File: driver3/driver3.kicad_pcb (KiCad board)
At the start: 4 copper layers, 45 x 60 mm, 23 parts, among them J1 Conn_02x08_Odd_Even, J2 Conn_02x08_Counter_Clockwise, J3 Conn_01x05, J4 Conn_01x03_Pin, SW1 SW_DIP_x02, SW2 SW_DIP_x02, U1 MP6605CGR-Z

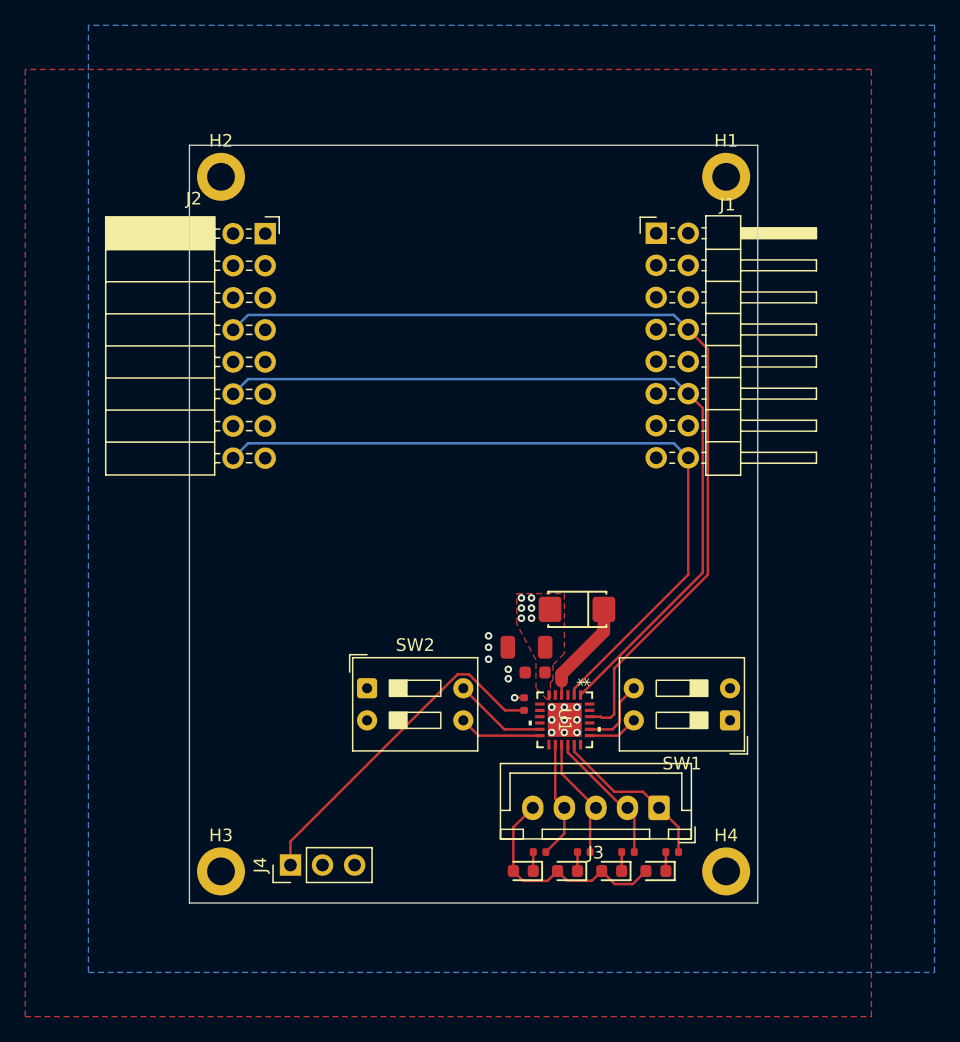
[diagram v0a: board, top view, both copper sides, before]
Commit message: Add new driver and web client
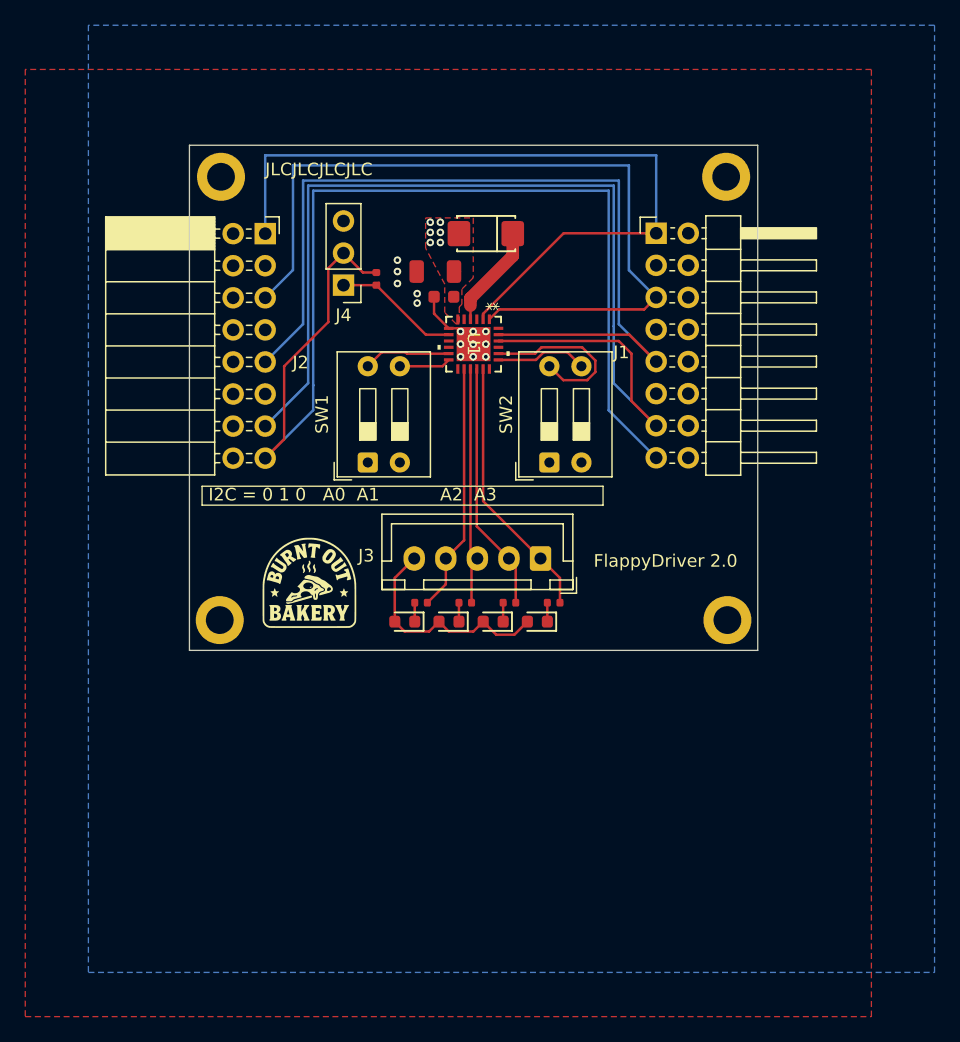
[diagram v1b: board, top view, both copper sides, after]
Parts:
- added G1: LOGO, BurntOutBakery:BurntOutBakery, F.Cu at (109.5, 85.0)
- J1: value Conn_02x08_Odd_Even -> Conn_02x08_Odd_Even_Male
- J2: value Conn_02x08_Counter_Clockwise -> Conn_02x08_Odd_Even_Female
- moved J4 46.1 mm to (112.2, 61.1), turned to 180 degrees
- moved R5 35.6 mm to (114.8, 60.6)
- moved C1 30.6 mm to (120.2, 62.0)
- moved C2 30.6 mm to (119.5, 60.0)
- moved D1 30.6 mm to (123.5, 57.0)
- moved U1 30.6 mm to (122.5, 65.8)
- moved SW2 24.9 mm to (128.5, 75.1), turned to 90 degrees
- moved D2 21.9 mm to (127.5, 87.7)
- moved D3 21.9 mm to (124.0, 87.7)
- moved D4 21.9 mm to (120.5, 87.7)
- moved J3 21.9 mm to (127.8, 82.7)
- moved D5 21.9 mm to (117.0, 87.7)
- moved R1 21.9 mm to (128.8, 86.2)
- moved R2 21.9 mm to (125.3, 86.2)
- moved R3 21.9 mm to (121.8, 86.2)
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- renumbered SW2 to SW1, SW1 to SW2
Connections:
- J1 pad 1: +12V -> SCL
- J1 pad 12: SDA -> +12V
- J1 pad 13: +12V -> NENBL
- J1 pad 15: GND -> +5V
- J1 pad 16: SCL -> +12V
- J1 pad 2: +5V -> GND
- J1 pad 4: NFAULT -> +12V
- J1 pad 5: +12V -> SDA
- J1 pad 8: NENBL -> +12V
- J1 pad 9: +12V -> NFAULT
- J2 pad 1: +12V -> SCL
- J2 pad 12: SDA -> +12V
- J2 pad 13: +12V -> NENBL
- J2 pad 15: GND -> +5V
- J2 pad 16: SCL -> +12V
- J2 pad 2: +5V -> GND
- J2 pad 4: NFAULT -> +12V
- J2 pad 5: +12V -> SDA
- J2 pad 8: NENBL -> +12V
- J2 pad 9: +12V -> NFAULT
- SW2 pad 3: A2 -> A3
- SW2 pad 4: A3 -> A2
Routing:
- net +5V: track 0.75 -> 90.9 mm, vias 1 -> 0
- net NFAULT: track 0.00 -> 69.5 mm
- net Net-(J4-Pin_1): track 27.0 -> 10.2 mm
- net Net-(J3-Pin_4): track 9.40 -> 19.7 mm
- net NENBL: track 73.3 -> 82.5 mm
- net Net-(J3-Pin_3): track 9.82 -> 18.9 mm
- net Net-(J3-Pin_2): track 10.9 -> 19.8 mm
- net A2: track 5.76 -> 13.6 mm
- net Net-(J3-Pin_1): track 13.2 -> 21.0 mm
- net GND: track 0.00 -> 5.47 mm
- net A3: track 4.00 -> 7.27 mm
- net A1: track 6.56 -> 4.08 mm
- net SDA: track 65.4 -> 63.3 mm
- net SCL: track 59.5 -> 60.1 mm
- added copper zone on B.Cu, net GND
- removed copper zone on B.Cu, net +5V
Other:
- board size 45 x 60 mm -> 45 x 40 mm
- board text added: "FlappyDriver 2.0"
- board text added: "I2C = 0 1 0 A0 A1 A2 A3"
- board text added: "JLCJLCJLCJLC"

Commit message: Go back to DRV8804 based design because the MP6605CGR seems to be out of stock.
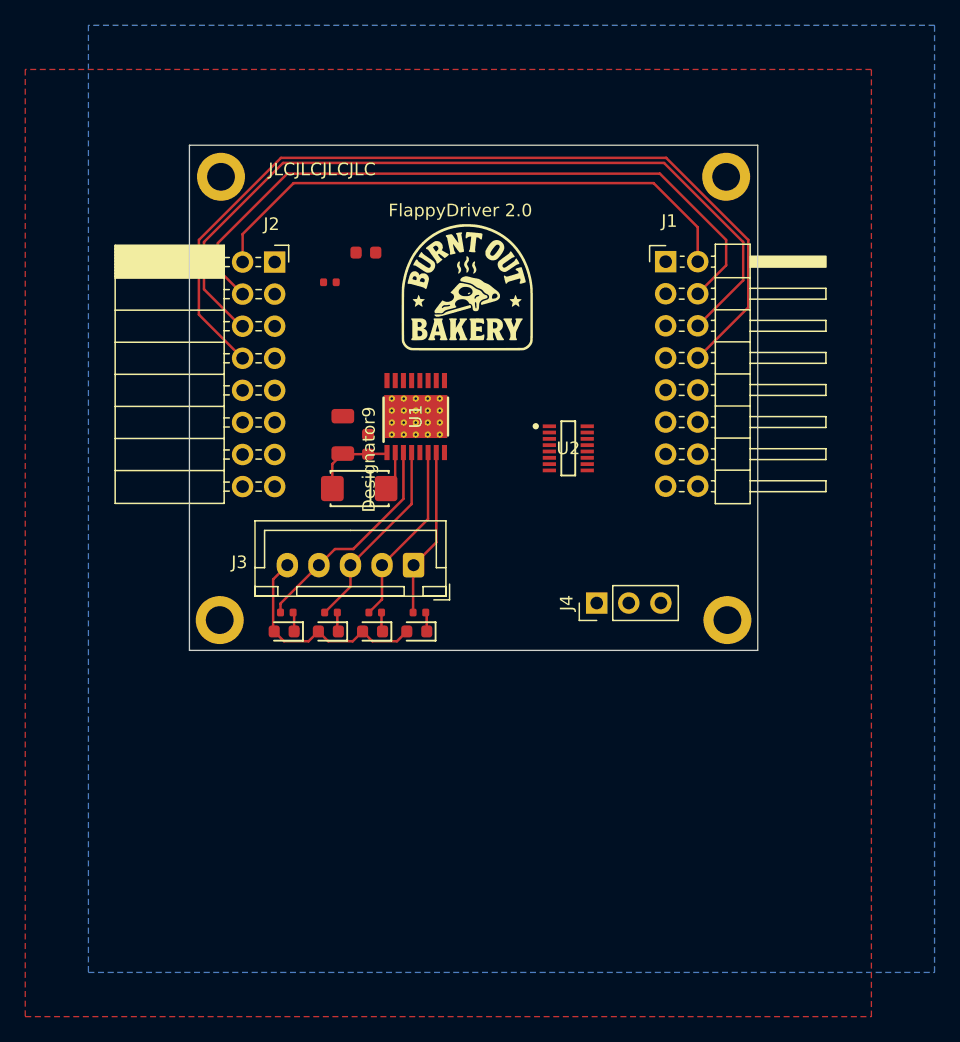
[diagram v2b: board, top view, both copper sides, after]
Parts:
- removed SW1, SW2: SW_DIP_x02, Button_Switch_THT:SW_DIP_SPSTx02_Slide_9.78x7.26mm_W7.62mm_P2.54mm
- added C3: 100nF, PCM_JLCPCB:C_0603, F.Cu at (114.0, 58.5)
- added U2: SN74HCS165DYYR, ul_SN74HCS165DYYR:DYY0016A-MFG, F.Cu at (130.0, 74.0)
- U1: value MP6605CGR-Z -> DRV8804PWP; footprint ul_MP6605CGR-Z:QFN-24_MP6605C_MNP -> ul_DRV8804PWP:PWP0016J_L
- moved J4 32.2 mm to (132.2, 86.2), turned to 90 degrees
- moved G1 26.4 mm to (122.0, 61.7)
- moved D1 22.5 mm to (113.4, 77.2)
- moved R1 21.1 mm to (107.7, 87.0), turned to 180 degrees
- moved D2 20.1 mm to (107.5, 88.5)
- moved C2 14.9 mm to (112.1, 72.9), turned to 90 degrees
- moved R2 14.2 mm to (111.2, 87.0), turned to 180 degrees
- moved C1 13.1 mm to (114.1, 73.7), turned to 90 degrees
- moved D3 13.1 mm to (111.0, 88.5)
- moved J3 10.1 mm to (117.8, 83.2)
- moved U1 7.34 mm to (117.9, 71.5), turned to 90 degrees
- moved R3 7.17 mm to (114.7, 87.0), turned to 180 degrees
- moved D4 6.10 mm to (114.5, 88.5)
- moved R5 3.69 mm to (111.1, 60.9), turned to 0 degrees
- moved J1 2.37 mm to (137.7, 59.2)
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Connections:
- J1 pad 1: SCL -> GND
- J1 pad 10: GND -> +12V
- J1 pad 13: NENBL -> GND
- J1 pad 14: GND -> +12V
- J1 pad 15: +5V -> +3V3
- J1 pad 2: GND -> unconnected-(J1-Pin_2-Pad2)
- J1 pad 4: +12V -> unconnected-(J1-Pin_4-Pad4)
- J1 pad 5: SDA -> GND
- J1 pad 6: GND -> unconnected-(J1-Pin_6-Pad6)
- J1 pad 8: +12V -> unconnected-(J1-Pin_8-Pad8)
- J1 pad 9: NFAULT -> GND
- J2 pad 1: SCL -> GND
- J2 pad 10: GND -> +12V
- J2 pad 13: NENBL -> GND
- J2 pad 14: GND -> +12V
- J2 pad 15: +5V -> +3V3
- J2 pad 2: GND -> unconnected-(J2-Pin_2-Pad2)
- J2 pad 4: +12V -> unconnected-(J2-Pin_4-Pad4)
- J2 pad 5: SDA -> GND
- J2 pad 6: GND -> unconnected-(J2-Pin_6-Pad6)
- J2 pad 8: +12V -> unconnected-(J2-Pin_8-Pad8)
- J2 pad 9: NFAULT -> GND
- J4 pad 1: Net-(J4-Pin_1) -> GND
- J4 pad 2: +5V -> +12V
- J4 pad 3: GND -> Net-(J4-Pin_3)
- R1 pad 2: Net-(J3-Pin_1) -> Net-(J3-Pin_4)
- R2 pad 2: Net-(J3-Pin_2) -> Net-(J3-Pin_3)
- R3 pad 2: Net-(J3-Pin_3) -> Net-(J3-Pin_2)
- R4 pad 2: Net-(J3-Pin_4) -> Net-(J3-Pin_1)
- R5 pad 1: +5V -> Net-(J4-Pin_3)
- R5 pad 2: Net-(J4-Pin_1) -> +3V3
- U1 pad 1: SDA -> +12V
- U1 pad 11: A0 -> LATCH
- U1 pad 12: A1 -> GND
- U1 pad 13: unconnected-(U1-NC-Pad13) -> SCLK
- U1 pad 14: Net-(J3-Pin_4) -> CO
- U1 pad 15: Net-(J3-Pin_3) -> PI
- U1 pad 16: Net-(J3-Pin_2) -> FAULT
- U1 pad 17: Net-(J3-Pin_1) -> GND
- U1 pad 2: SCL -> Net-(U1-VCLAMP)
- U1 pad 3: unconnected-(U1-NC-Pad3) -> Net-(J3-Pin_4)
- U1 pad 4: Net-(U1-VCLAMP) -> Net-(J3-Pin_3)
- U1 pad 5: unconnected-(U1-NC-Pad5) -> GND
- U1 pad 6: +12V -> Net-(J3-Pin_2)
- U1 pad 7: GND -> Net-(J3-Pin_1)
- U1 pad 8: Net-(J4-Pin_1) -> NENBL
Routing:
- net (no net): track 0.00 -> 162.9 mm
- net +5V: track 90.9 -> 0.00 mm
- net NFAULT: track 69.5 -> 0.00 mm
- net SDA: track 63.3 -> 0.00 mm
- net SCL: track 60.1 -> 0.00 mm
- net A2: track 13.6 -> 0.00 mm
- net NENBL: track 82.5 -> 70.7 mm
- net Net-(J4-Pin_1): track 10.2 -> 0.00 mm
- net Net-(J3-Pin_1): track 21.0 -> 13.3 mm
- net A3: track 7.27 -> 0.00 mm
- net A0: track 6.91 -> 0.00 mm
- net +12V: track 18.7 -> 24.8 mm, vias 6 -> 0
- net GND: track 5.47 -> 0.04 mm, vias 14 -> 0
- net Net-(J3-Pin_2): track 19.8 -> 14.5 mm
- net Net-(U1-VCLAMP): track 8.17 -> 3.05 mm
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- added copper zone on In2.Cu, net +12V
- added copper zone on B.Cu, net +3V3
- added copper zone on In1.Cu, net GND
- removed copper zone on F.Cu, net +12V
- removed copper zone on In1.Cu, net +12V
- removed copper zone on B.Cu, net GND
- removed copper zone on In2.Cu, net GND
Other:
- board text removed: "I2C = 0 1 0 A0 A1 A2 A3"

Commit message: Add picotool reset support.
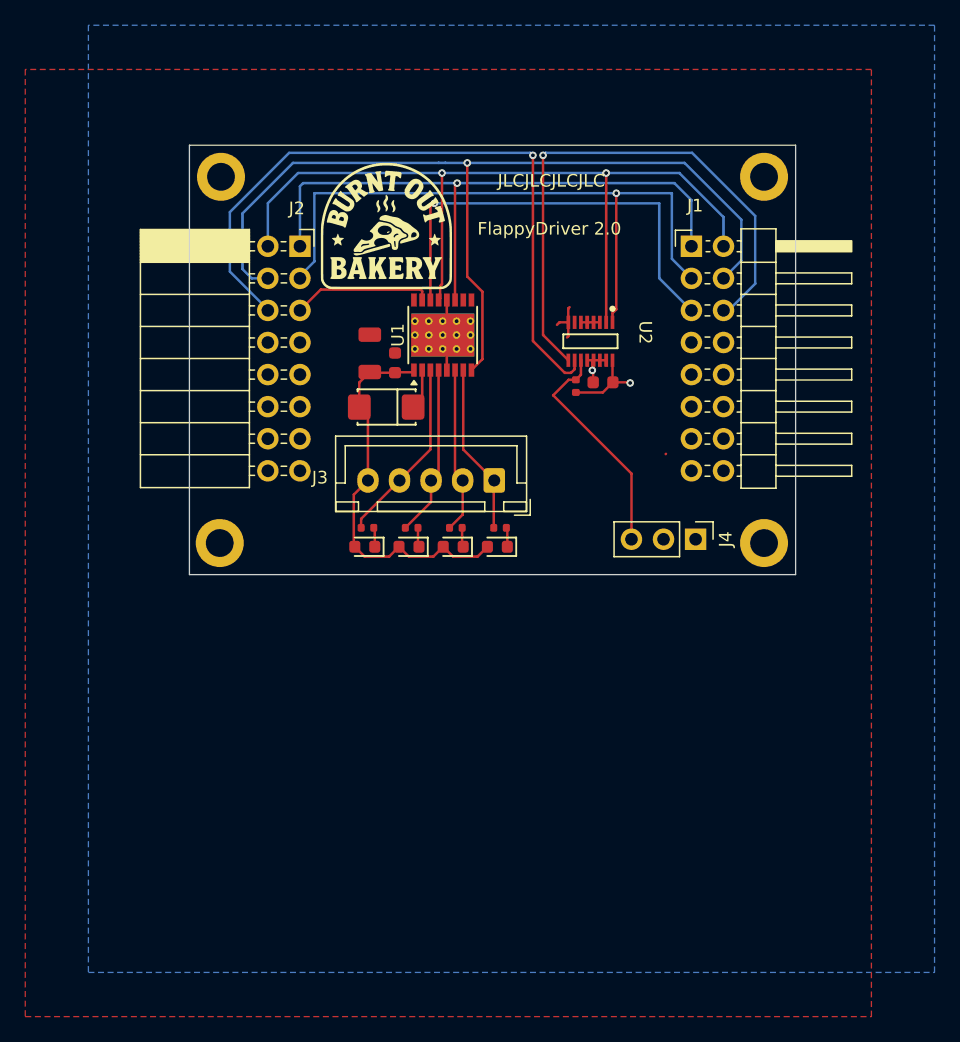
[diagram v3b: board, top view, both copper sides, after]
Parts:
- U1: footprint ul_DRV8804PWP:PWP0016J_L -> Package_SO:HTSSOP-16-1EP_4.4x5mm_P0.65mm_EP3.4x5mm_Mask3x3mm_ThermalVias
- moved C3 21.4 mm to (132.8, 68.8), turned to 180 degrees
- moved R5 21.1 mm to (130.6, 69.1), turned to -90 degrees
- moved J4 9.32 mm to (140.1, 81.2), turned to -90 degrees
- moved D2 9.26 mm to (113.9, 81.8)
- moved D3 9.26 mm to (117.4, 81.8)
- moved D4 9.26 mm to (120.9, 81.8)
- moved D5 9.26 mm to (124.4, 81.8)
- moved J3 9.26 mm to (124.1, 76.5)
- moved R1 9.26 mm to (114.1, 80.3)
- moved R2 9.26 mm to (117.6, 80.3)
- moved R3 9.26 mm to (121.1, 80.3)
- moved R4 9.26 mm to (124.6, 80.3)
- moved U2 8.65 mm to (131.8, 65.5), turned to -90 degrees
- moved G1 8.03 mm to (115.6, 56.9)
- moved C1 6.80 mm to (116.3, 67.2)
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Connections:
- J1 pad 1: GND -> LATCH
- J1 pad 15: +3V3 -> GND
- J1 pad 16: +12V -> +3V3
- J1 pad 2: unconnected-(J1-Pin_2-Pad2) -> SCLK
- J1 pad 3: GND -> LOAD
- J1 pad 4: unconnected-(J1-Pin_4-Pad4) -> NENBL
- J1 pad 5: GND -> CO
- J1 pad 6: unconnected-(J1-Pin_6-Pad6) -> CI
- J1 pad 7: GND -> unconnected-(J1-Pin_7-Pad7)
- J2 pad 1: GND -> LATCH
- J2 pad 15: +3V3 -> GND
- J2 pad 16: +12V -> +3V3
- J2 pad 2: unconnected-(J2-Pin_2-Pad2) -> SCLK
- J2 pad 3: GND -> LOAD
- J2 pad 4: unconnected-(J2-Pin_4-Pad4) -> NENBL
- J2 pad 5: GND -> PI
- J2 pad 6: unconnected-(J2-Pin_6-Pad6) -> PO
- J2 pad 7: GND -> unconnected-(J2-Pin_7-Pad7)
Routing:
- net (no net): track 162.9 -> 0.00 mm
- net SCLK: track 0.00 -> 66.2 mm, vias 0 -> 2
- net PO: track 0.00 -> 54.9 mm, vias 0 -> 1
- net LOAD: track 0.00 -> 53.2 mm, vias 0 -> 1
- net LATCH: track 0.00 -> 49.4 mm, vias 0 -> 1
- net CI: track 0.00 -> 44.8 mm, vias 0 -> 1
- net CO: track 0.00 -> 35.2 mm, vias 0 -> 1
- net Net-(J4-Pin_3): track 0.00 -> 18.0 mm
- net GND: track 0.04 -> 14.1 mm, vias 0 -> 1
- net PI: track 0.00 -> 11.1 mm
- net +3V3: track 0.00 -> 6.41 mm, vias 0 -> 1
- net +12V: track 24.8 -> 30.9 mm
- net Net-(J3-Pin_4): track 17.4 -> 14.8 mm
- net Net-(J3-Pin_3): track 15.4 -> 13.6 mm
- net NENBL: track 70.7 -> 72.2 mm, vias 0 -> 1
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- added copper zone on In1.Cu, net +12V
- added copper zone on In2.Cu, net GND
- removed copper zone on In2.Cu, net +12V
- removed copper zone on In1.Cu, net GND
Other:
- board size 45 x 40 mm -> 48 x 34 mm
